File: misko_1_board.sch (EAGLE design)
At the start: 152 parts, among them IC1 ATMEGA1281-16AU, IC10 ORG1510-MK4, IC11 TPS3808G33DBVT, IC12 LTC4425, IC13 RN4678_BT_MODULE, IC14 ADXL345, IC15 74HCT1G32, IC16 FM25W256-SOIC, IC17 MICROSD_SPI_MODE, IC18 FH12-30S-0.5SH, IC19 DS1394U-33+, IC2 MC1525TT, IC20 ATWINC1500-MR210PB, IC21 115Q-BCA0, IC22 SIM800, IC3 TMP36GRTZ, IC4 TPS63031, IC5 MCP73871-2AAI/ML, IC6 MAX6818, IC7 FT230XS, IC8 SN74LVC1G3157DBVR - BT switch, IC9 SN74LVC1G3157DBVR - GPS switch, Q1 ABM3B-8MHZ-10-1-U-T, Q2 LFXTAL016178R, SW1 RESET, SW2 POWER SWITCH, SW3 MICROJOYSTICK, SW4 PB6156RSL, SW5 PB6156RSL, T1 BSS84

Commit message: - cleaned up up the GPS module's library
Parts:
- R2: value 150k -> 10k
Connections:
- net GND: now also IC10.GND; no longer IC10.GND1, IC10.GND2, IC10.GND3, IC10.GND4, IC10.GND5
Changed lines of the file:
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@@
 <part name="C25" library="EECS5R5H155 Supercap" deviceset="EECS5R5H155" device="" value="1.5F"/>
 <part name="IC4" library="TPS63031 - Buck Boost Voltage Regulator" deviceset="TPS63001DRCR" device="" value="TPS63031"/>
-<part name="R2" library="resistor" library_urn="urn:adsk.eagle:library:348" deviceset="R-EU_" device="R0805" value="150k"/>
+<part name="R2" library="resistor" library_urn="urn:adsk.eagle:library:348" deviceset="R-EU_" device="R0805" value="10k"/>
 <part name="C11" library="rcl" deviceset="C-EU" device="C0805" value="22µF"/>
 <part name="C6" library="rcl" deviceset="C-EU" device="C0805" value="10µF"/>
@@
 <part name="C38" library="rcl" library_urn="urn:adsk.eagle:library:334" deviceset="CPOL-EU" device="E5-10.5" value="1000µF"/>
 <part name="D2" library="diode" library_urn="urn:adsk.eagle:library:210" deviceset="BAT60J" device="" value=" BAT60AE6327 "/>
-<part name="IC10" library="ORG1510-MK4 GPS module" deviceset="ORG1510-MK4" device=""/>
 <part name="SW1" library="Wurth_Elektronik_Electromechanic_Switch_rev17c" library_urn="urn:adsk.eagle:library:480" deviceset="430152050836" device="" value="RESET"/>
 <part name="Q1" library="ABM3B-8MHZ-10-1-U-T - Quartz Resonator" deviceset="ABM3B" device="" value="ABM3B-8MHZ-10-1-U-T"/>
@@
 <part name="D7" library="zener" library_urn="urn:adsk.eagle:library:449000" deviceset="ZENER" device="" value="BZG05C3V6-E3-TR3"/>
 <part name="R23" library="resistor" library_urn="urn:adsk.eagle:library:348" deviceset="R-EU_" device="R0805" value="10k"/>
+<part name="IC10" library="ORG1510-MK4 GPS module" deviceset="ORG1510-MK4" device="" value="ORG1510-MK4"/>
 </parts>
 <sheets>
@@
 <instance part="C38" gate="G$1" x="322.58" y="472.44"/>
 <instance part="D2" gate="G$1" x="261.62" y="474.98"/>
-<instance part="IC10" gate="G$1" x="48.26" y="38.1"/>
 <instance part="SW1" gate="G$1" x="22.86" y="650.24" rot="R90"/>
 <instance part="Q1" gate="G$1" x="101.6" y="642.62"/>
@@
 </instance>
 <instance part="R23" gate="G$1" x="149.86" y="66.04" rot="R90"/>
+<instance part="IC10" gate="G$1" x="58.42" y="43.18"/>
 </instances>
 <busses>
@@
 </segment>
 <segment>
-<wire x1="53.34" y1="22.86" x2="55.88" y2="22.86" width="0.1524" layer="91"/>
-<wire x1="55.88" y1="22.86" x2="58.42" y2="22.86" width="0.1524" layer="91"/>
-<wire x1="58.42" y1="22.86" x2="60.96" y2="22.86" width="0.1524" layer="91"/>
-<wire x1="60.96" y1="22.86" x2="63.5" y2="22.86" width="0.1524" layer="91"/>
+<wire x1="58.42" y1="22.86" x2="63.5" y2="22.86" width="0.1524" layer="91"/>
 <wire x1="63.5" y1="22.86" x2="63.5" y2="17.78" width="0.1524" layer="91"/>
 <label x="63.5" y="17.78" size="1.778" layer="95"/>
-<pinref part="IC10" gate="G$1" pin="GND1"/>
-<pinref part="IC10" gate="G$1" pin="GND2"/>
-<junction x="55.88" y="22.86"/>
-<pinref part="IC10" gate="G$1" pin="GND3"/>
-<junction x="58.42" y="22.86"/>
-<pinref part="IC10" gate="G$1" pin="GND4"/>
-<junction x="60.96" y="22.86"/>
-<pinref part="IC10" gate="G$1" pin="GND5"/>
-<junction x="63.5" y="22.86"/>
-</segment>
-<segment>
+<pinref part="IC10" gate="G$1" pin="GND"/>
+</segment>
+<segment>

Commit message: - aligned tplace/bplace stuff to grid
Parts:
- D3: value BZT52C5V1-E3-18 -> SZ1SMB5916BT3G; device zener:ZENERSOD123 -> diode:DIODE-SMB
- D4: value BZT52C3V3-E3-08 -> SZ1SMB5916BT3G; device zener:ZENERSOD123 -> diode:DIODE-SMB
- D5: value BZT52C4V3-E3-18 -> SZ1SMB5916BT3G; device zener:ZENERSOD123 -> diode:DIODE-SMB
- D6: value 1N4733AW-TP -> SMBJ5339B-TP; device zener:ZENERSOD123 -> diode:DIODE-DO214AA
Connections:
- net 5V0: now also D6.C; no longer D6.CAT
- net GND: now also D3.A, D4.A, D5.A, D6.A; no longer D3.AN, D4.AN, D5.AN, D6.AN
- net VCC: now also D4.C; no longer D4.CAT
- net V_LIION+: now also D3.C, D5.C; no longer D3.CAT, D5.CAT

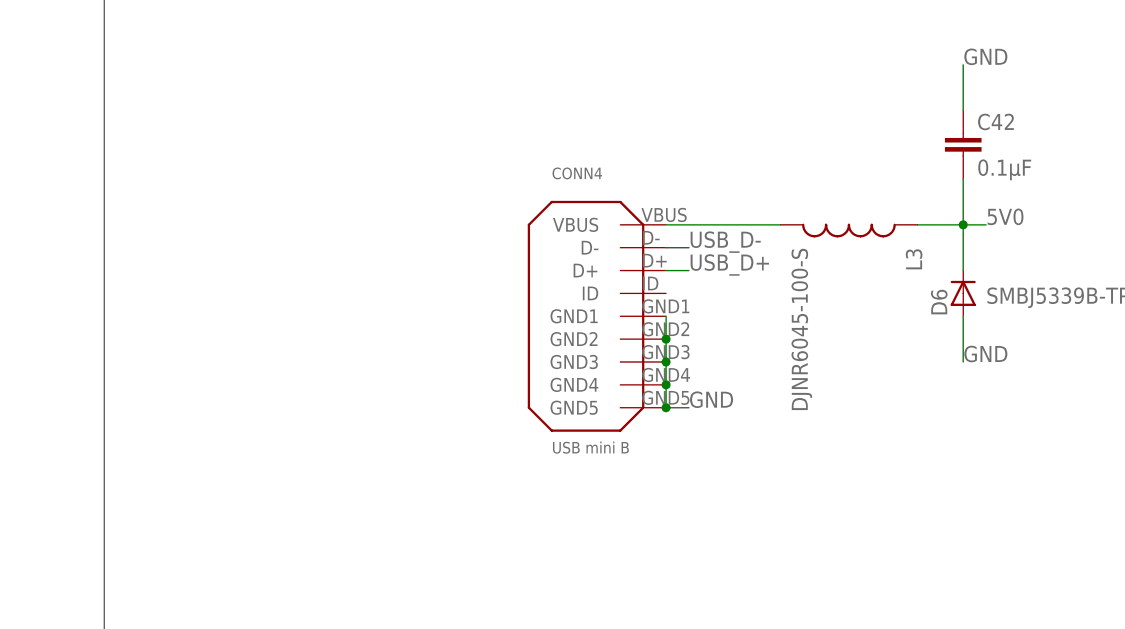
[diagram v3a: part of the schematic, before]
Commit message: - added SP3012 TVS Diode Array.lbr into schematic and routed element to USB port
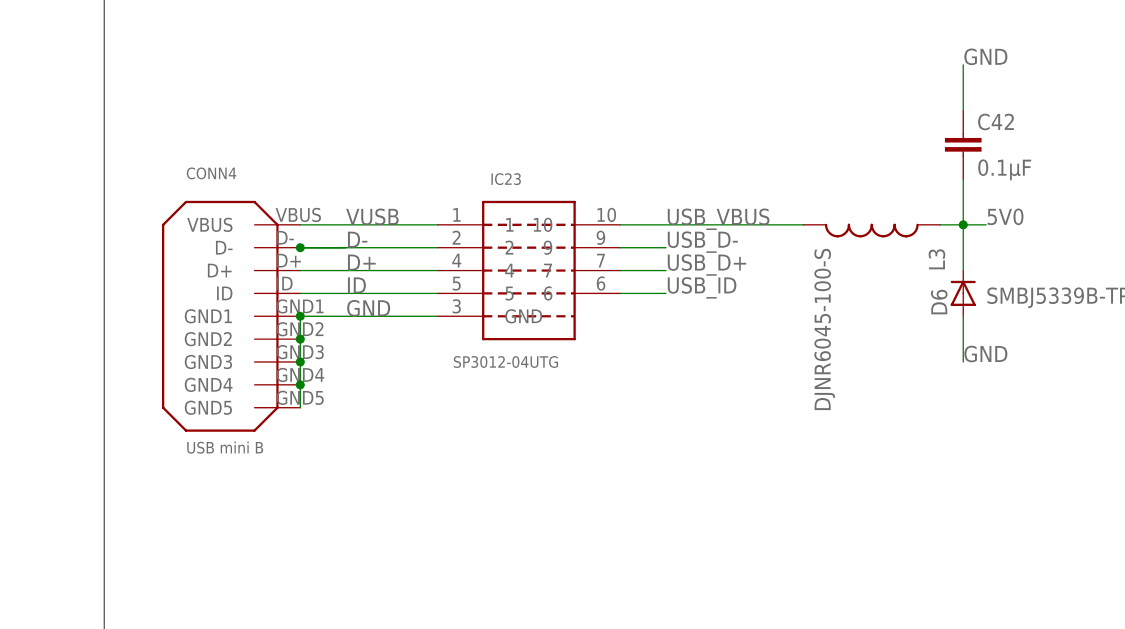
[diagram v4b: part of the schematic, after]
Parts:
- added IC23: SP3012-04UTG, SP3012 TVS Diode Array:SP3012-04UTG
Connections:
- new net D+: CONN4.D+, IC23.4
- new net D-: CONN4.D-, IC23.2
- new net ID: CONN4.ID, IC23.5
- new net USB_ID: IC23.6
- new net USB_VBUS: IC23.10, L3.2
- net GND: now also IC23.GND
- net USB_D+: now also IC23.7; no longer CONN4.D+
- net USB_D-: now also IC23.9; no longer CONN4.D-
- net VUSB: now also IC23.1; no longer L3.2
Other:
- moved on the sheet: CONN4, L3

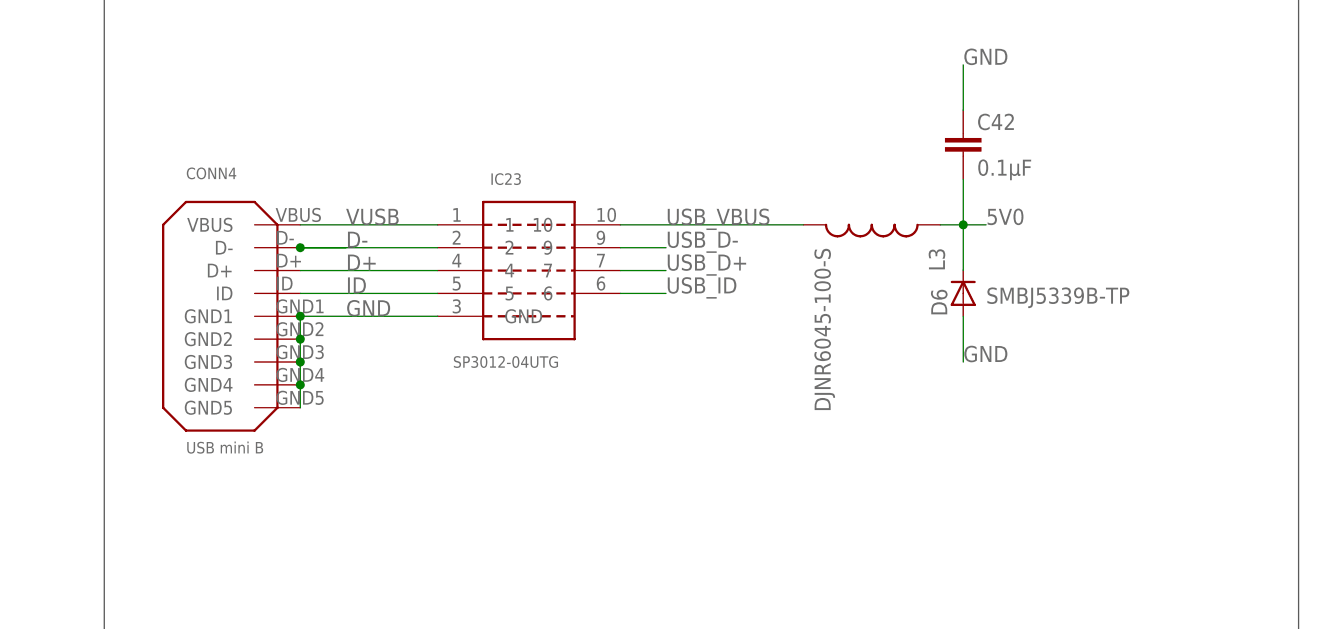
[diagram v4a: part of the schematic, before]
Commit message: - removed UDB inductor and protection diode - added PTS1206-Series Polyfuse
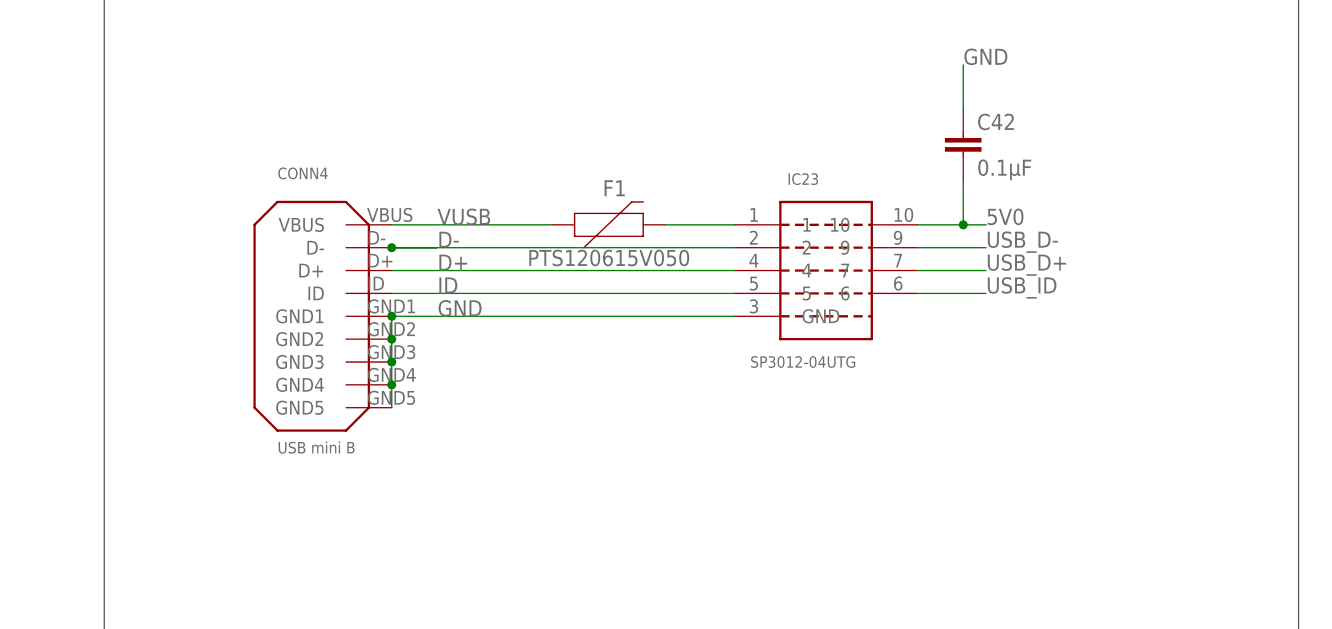
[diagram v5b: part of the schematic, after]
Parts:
- removed D6: SMBJ5339B-TP, diode:DIODE-DO214AA
- removed L3: DJNR6045-100-S, DJNR6045-100S Power Inductor:DJNR6045-100-S
- added F1: PTS120615V050, SparkFun-Fuses:PPTC_THREE-QUARTER-AMP
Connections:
- removed net USB_VBUS: IC23.10, L3.2
- new net N$4: F1.2, IC23.1
- net 5V0: now also IC23.10; no longer D6.C, L3.1
- net GND: no longer D6.A
- net VUSB: now also F1.1; no longer IC23.1
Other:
- moved on the sheet: CONN4, IC23
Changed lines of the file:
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@@
 <part name="TP4" library="testpad" deviceset="PTR1" device="TP14R" value="VCC"/>
 <part name="TP1" library="testpad" deviceset="TP" device="PAD1-17Y" value="GND"/>
-<part name="L3" library="DJNR6045-100S Power Inductor" deviceset="DJNR6045-100-S" device=""/>
 <part name="C42" library="resistor" library_urn="urn:adsk.eagle:library:348" deviceset="C-EU" device="C0805" value="0.1µF"/>
 <part name="IC18" library="con-hirose" deviceset="FH12-30S-0.5S" device="H"/>
@@
 <part name="D5" library="diode" library_urn="urn:adsk.eagle:library:210" deviceset="DIODE-" device="SMB" package3d_urn="urn:adsk.eagle:package:43404/2" value="SZ1SMB5916BT3G"/>
 <part name="D4" library="diode" library_urn="urn:adsk.eagle:library:210" deviceset="DIODE-" device="SMB" package3d_urn="urn:adsk.eagle:package:43404/2" value="SZ1SMB5916BT3G"/>
-<part name="D6" library="diode" library_urn="urn:adsk.eagle:library:210" deviceset="DIODE-" device="DO214AA" package3d_urn="urn:adsk.eagle:package:43433/2" value="SMBJ5339B-TP"/>
 <part name="D7" library="zener" library_urn="urn:adsk.eagle:library:449000" deviceset="ZENER" device="" value="BZG05C3V6-E3-TR3"/>
 <part name="R23" library="resistor" library_urn="urn:adsk.eagle:library:348" deviceset="R-EU_" device="R0805" value="10k"/>
 <part name="IC10" library="ORG1510-MK4 GPS module" deviceset="ORG1510-MK4" device="" value="ORG1510-MK4"/>
 <part name="IC23" library="SP3012 TVS Diode Array" deviceset="SP3012-04UTG" device="" value="SP3012-04UTG"/>
+<part name="F1" library="SparkFun-Fuses" library_urn="urn:adsk.eagle:library:517" deviceset="PPTC" device="_THREE-QUARTER-AMP" package3d_urn="urn:adsk.eagle:package:38575/1" value="PTS120615V050 "/>
 </parts>
 <sheets>
@@
 <attribute name="TP_SIGNAL_NAME" x="267.94" y="805.26" size="1.778" layer="97" rot="R90"/>
 </instance>
-<instance part="L3" gate="G$2" x="322.58" y="220.98" rot="R270"/>
 <instance part="C42" gate="G$1" x="332.74" y="231.14"/>
 <instance part="IC18" gate="-1" x="55.88" y="-215.9"/>
@@
 <instance part="SW1" gate="G$1" x="22.86" y="650.24" rot="R90"/>
 <instance part="Q1" gate="G$1" x="101.6" y="642.62"/>
-<instance part="CONN4" gate="G$1" x="254" y="215.9"/>
+<instance part="CONN4" gate="G$1" x="264.16" y="215.9"/>
 <instance part="TP2" gate="G$1" x="266.67" y="798.91" smashed="yes" rot="R90">
 <attribute name="NAME" x="260.684" y="798.352" size="1.778" layer="95"/>
@@
 <attribute name="VALUE" x="167.64" y="-11.303" size="1.778" layer="96"/>
 </instance>
-<instance part="D6" gate="G$1" x="332.74" y="213.36" smashed="yes" rot="R90">
-<attribute name="NAME" x="330.962" y="210.82" size="1.778" layer="95" rot="R90"/>
-<attribute name="VALUE" x="335.28" y="212.217" size="1.778" layer="96"/>
-</instance>
 <instance part="D7" gate="G$1" x="111.76" y="523.24" smashed="yes" rot="R270">
 <attribute name="NAME" x="113.538" y="525.78" size="1.778" layer="95" rot="R270"/>
@@
 <instance part="R23" gate="G$1" x="149.86" y="66.04" rot="R90"/>
 <instance part="IC10" gate="G$1" x="58.42" y="43.18"/>
-<instance part="IC23" gate="G$1" x="284.48" y="215.9"/>
+<instance part="IC23" gate="G$1" x="317.5" y="215.9"/>
+<instance part="F1" gate="G$1" x="292.1" y="220.98"/>
 </instances>
 <busses>
@@
 <pinref part="CONN4" gate="G$1" pin="GND1"/>
 <pinref part="CONN4" gate="G$1" pin="GND2"/>
-<wire x1="259.08" y1="210.82" x2="259.08" y2="208.28" width="0.1524" layer="91"/>
+<wire x1="269.24" y1="210.82" x2="269.24" y2="208.28" width="0.1524" layer="91"/>
 <pinref part="CONN4" gate="G$1" pin="GND3"/>
-<wire x1="259.08" y1="208.28" x2="259.08" y2="205.74" width="0.1524" layer="91"/>
-<junction x="259.08" y="208.28"/>
+<wire x1="269.24" y1="208.28" x2="269.24" y2="205.74" width="0.1524" layer="91"/>
+<junction x="269.24" y="208.28"/>
 <pinref part="CONN4" gate="G$1" pin="GND4"/>
-<wire x1="259.08" y1="205.74" x2="259.08" y2="203.2" width="0.1524" layer="91"/>
-<junction x="259.08" y="205.74"/>
+<wire x1="269.24" y1="205.74" x2="269.24" y2="203.2" width="0.1524" layer="91"/>
+<junction x="269.24" y="205.74"/>
 <pinref part="CONN4" gate="G$1" pin="GND5"/>
-<wire x1="259.08" y1="203.2" x2="259.08" y2="200.66" width="0.1524" layer="91"/>
-<junction x="259.08" y="203.2"/>
-<label x="264.16" y="210.82" size="1.778" layer="95"/>
+<wire x1="269.24" y1="203.2" x2="269.24" y2="200.66" width="0.1524" layer="91"/>
+<junction x="269.24" y="203.2"/>
+<label x="274.32" y="210.82" size="1.778" layer="95"/>
 <pinref part="IC23" gate="G$1" pin="GND"/>
-<wire x1="259.08" y1="210.82" x2="274.32" y2="210.82" width="0.1524" layer="91"/>
-<junction x="259.08" y="210.82"/>
+<wire x1="269.24" y1="210.82" x2="307.34" y2="210.82" width="0.1524" layer="91"/>
+<junction x="269.24" y="210.82"/>
 </segment>
 <segment>
@@
 </segment>
 <segment>
-<pinref part="D6" gate="G$1" pin="A"/>
-<wire x1="332.74" y1="210.82" x2="332.74" y2="205.74" width="0.1524" layer="91"/>
-<label x="332.74" y="205.74" size="1.778" layer="95"/>
-</segment>
-<segment>
 <pinref part="D7" gate="G$1" pin="AN"/>
 <wire x1="111.76" y1="525.78" x2="111.76" y2="535.94" width="0.1524" layer="91"/>
@@
 <segment>
 <pinref part="C42" gate="G$1" pin="2"/>
-<wire x1="330.2" y1="220.98" x2="332.74" y2="220.98" width="0.1524" layer="91"/>
 <label x="335.28" y="220.98" size="1.778" layer="95"/>
-<pinref part="L3" gate="G$2" pin="1"/>
 <wire x1="332.74" y1="220.98" x2="335.28" y2="220.98" width="0.1524" layer="91"/>
 <wire x1="332.74" y1="226.06" x2="332.74" y2="220.98" width="0.1524" layer="91"/>
 <junction x="332.74" y="220.98"/>
-<pinref part="D6" gate="G$1" pin="C"/>
-<wire x1="332.74" y1="215.9" x2="332.74" y2="220.98" width="0.1524" layer="91"/>
+<wire x1="332.74" y1="220.98" x2="327.66" y2="220.98" width="0.1524" layer="91"/>
+<pinref part="IC23" gate="G$1" pin="10"/>
 </segment>
 <segment>
@@
 <segment>
 <pinref part="IC23" gate="G$1" pin="9"/>
-<wire x1="294.64" y1="218.44" x2="299.72" y2="218.44" width="0.1524" layer="91"/>
-<label x="299.72" y="218.44" size="1.778" layer="95"/>
+<wire x1="327.66" y1="218.44" x2="335.28" y2="218.44" width="0.1524" layer="91"/>
+<label x="335.28" y="218.44" size="1.778" layer="95"/>
 </segment>
 </net>
@@
 <segment>
 <pinref part="IC23" gate="G$1" pin="7"/>
-<wire x1="294.64" y1="215.9" x2="299.72" y2="215.9" width="0.1524" layer="91"/>
-<label x="299.72" y="215.9" size="1.778" layer="95"/>
+<wire x1="327.66" y1="215.9" x2="335.28" y2="215.9" width="0.1524" layer="91"/>
+<label x="335.28" y="215.9" size="1.778" layer="95"/>
 </segment>
 </net>
@@
 <segment>
 <pinref part="CONN4" gate="G$1" pin="VBUS"/>
-<pinref part="IC23" gate="G$1" pin="1"/>
-<wire x1="274.32" y1="220.98" x2="259.08" y2="220.98" width="0.1524" layer="91"/>
-<label x="264.16" y="220.98" size="1.778" layer="95"/>
+<label x="274.32" y="220.98" size="1.778" layer="95"/>
+<pinref part="F1" gate="G$1" pin="1"/>
+<wire x1="287.02" y1="220.98" x2="269.24" y2="220.98" width="0.1524" layer="91"/>
 </segment>
 <segment>
@@
 </segment>
 </net>
-<net name="USB_VBUS" class="1">
-<segment>
-<pinref part="L3" gate="G$2" pin="2"/>
-<wire x1="314.96" y1="220.98" x2="294.64" y2="220.98" width="0.1524" layer="91"/>
-<pinref part="IC23" gate="G$1" pin="10"/>
-<label x="299.72" y="220.98" size="1.778" layer="95"/>
-</segment>
-</net>
 <net name="USB_ID" class="0">
 <segment>
 <pinref part="IC23" gate="G$1" pin="6"/>
-<wire x1="294.64" y1="213.36" x2="299.72" y2="213.36" width="0.1524" layer="91"/>
-<label x="299.72" y="213.36" size="1.778" layer="95"/>
+<wire x1="327.66" y1="213.36" x2="335.28" y2="213.36" width="0.1524" layer="91"/>
+<label x="335.28" y="213.36" size="1.778" layer="95"/>
 </segment>
 </net>
@@
 <segment>
 <pinref part="IC23" gate="G$1" pin="5"/>
-<label x="264.16" y="213.36" size="1.778" layer="95"/>
+<label x="274.32" y="213.36" size="1.778" layer="95"/>
 <pinref part="CONN4" gate="G$1" pin="ID"/>
-<wire x1="259.08" y1="213.36" x2="274.32" y2="213.36" width="0.1524" layer="91"/>
+<wire x1="269.24" y1="213.36" x2="307.34" y2="213.36" width="0.1524" layer="91"/>
 </segment>
 </net>
@@
 <segment>
 <pinref part="CONN4" gate="G$1" pin="D-"/>
-<wire x1="259.08" y1="218.44" x2="264.16" y2="218.44" width="0.1524" layer="91"/>
-<label x="264.16" y="218.44" size="1.778" layer="95"/>
+<wire x1="269.24" y1="218.44" x2="274.32" y2="218.44" width="0.1524" layer="91"/>
+<label x="274.32" y="218.44" size="1.778" layer="95"/>
 <pinref part="IC23" gate="G$1" pin="2"/>
-<wire x1="274.32" y1="218.44" x2="259.08" y2="218.44" width="0.1524" layer="91"/>
-<junction x="259.08" y="218.44"/>
+<wire x1="307.34" y1="218.44" x2="269.24" y2="218.44" width="0.1524" layer="91"/>
+<junction x="269.24" y="218.44"/>
 </segment>
 </net>
@@
 <segment>
 <pinref part="CONN4" gate="G$1" pin="D+"/>
-<wire x1="259.08" y1="215.9" x2="274.32" y2="215.9" width="0.1524" layer="91"/>
-<label x="264.16" y="215.9" size="1.778" layer="95"/>
+<wire x1="269.24" y1="215.9" x2="307.34" y2="215.9" width="0.1524" layer="91"/>
+<label x="274.32" y="215.9" size="1.778" layer="95"/>
 <pinref part="IC23" gate="G$1" pin="4"/>
 </segment>
 </net>
+<net name="N$4" class="1">
+<segment>
+<pinref part="IC23" gate="G$1" pin="1"/>
+<wire x1="307.34" y1="220.98" x2="299.72" y2="220.98" width="0.1524" layer="91"/>
+<pinref part="F1" gate="G$1" pin="2"/>
+</segment>
+</net>

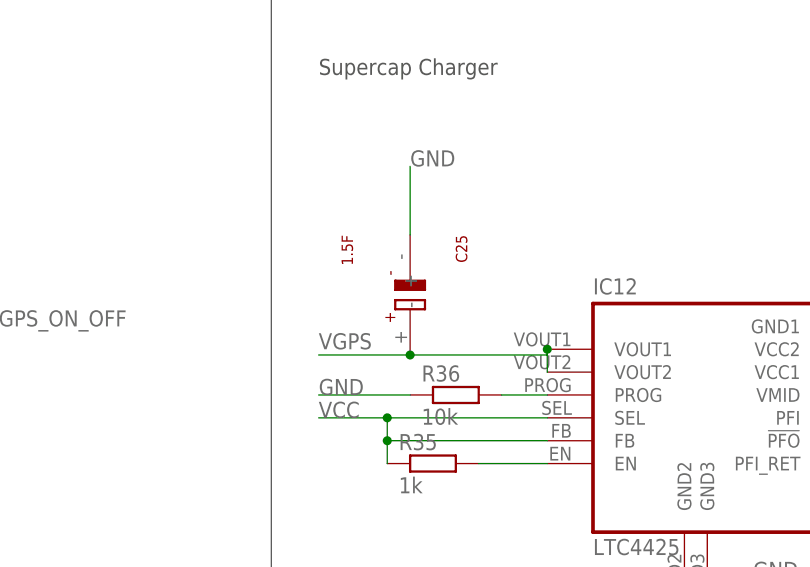
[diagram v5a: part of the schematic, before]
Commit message: - added "+" and "-" symbols for 5V0 connector
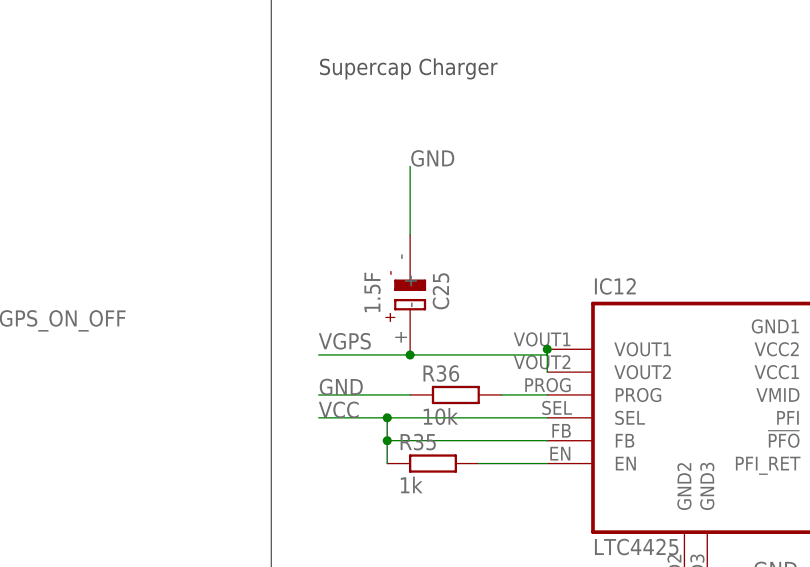
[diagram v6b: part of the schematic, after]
